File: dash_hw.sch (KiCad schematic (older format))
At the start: 25 parts, among them J1 Conn_01x06_Male, SW1 SW_Push, U1 STM32F103C8Tx, Y1 Crystal

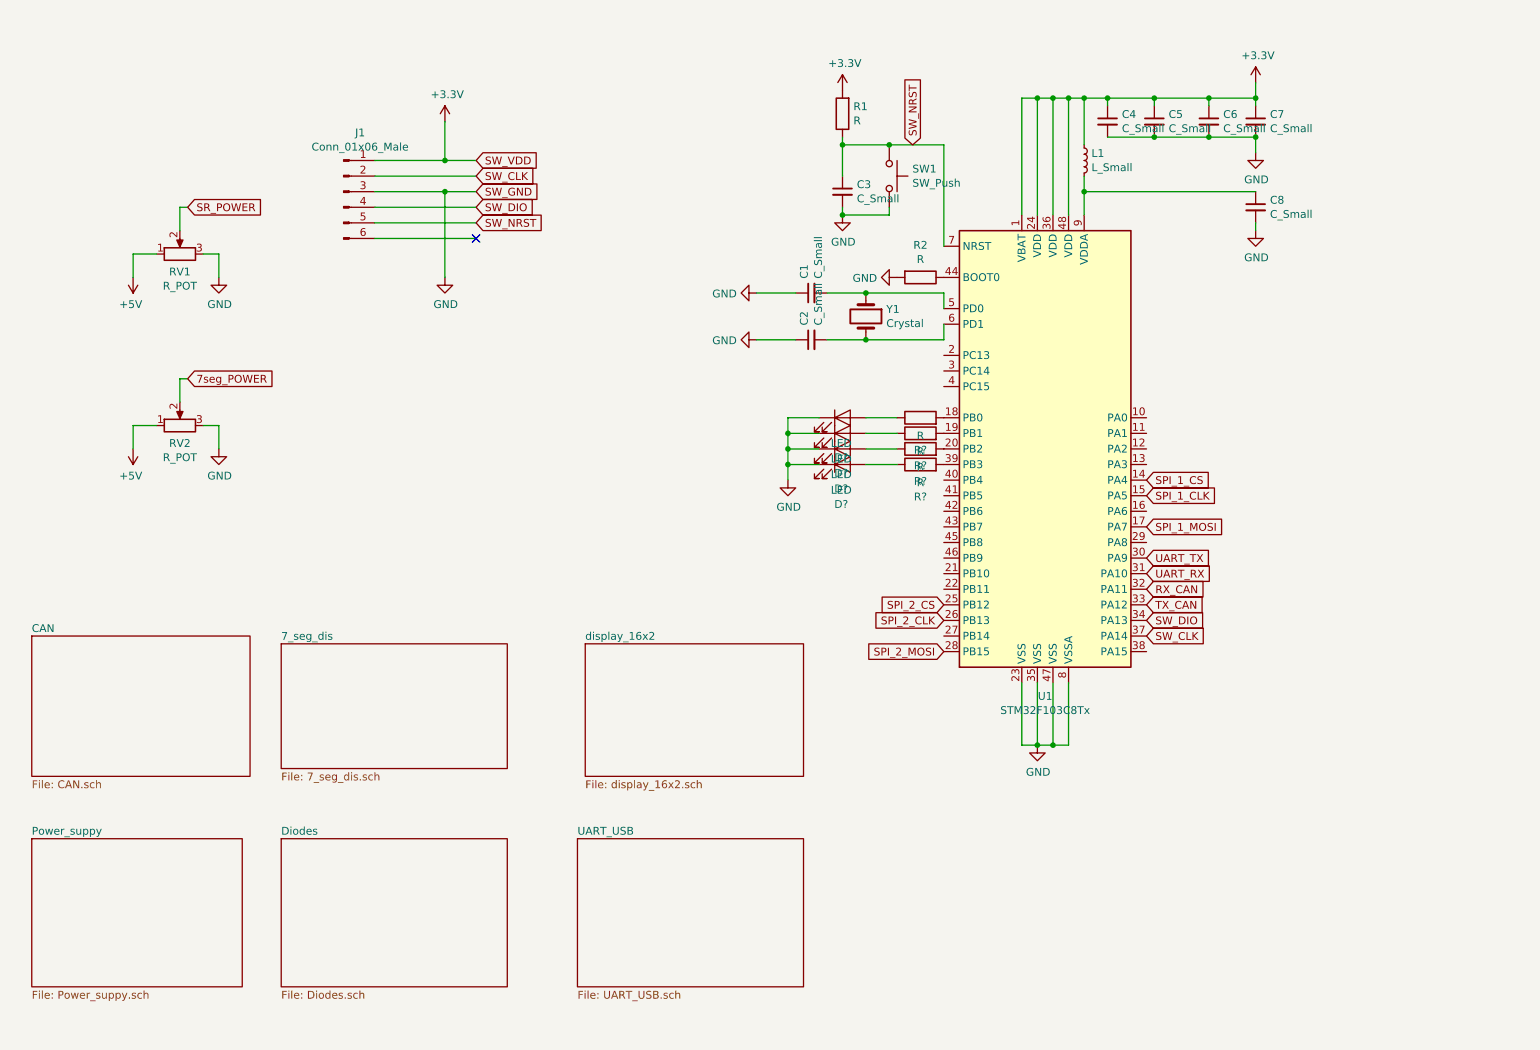
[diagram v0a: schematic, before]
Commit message: reorganized schematic; added reverse polarity protection; start adding footprints
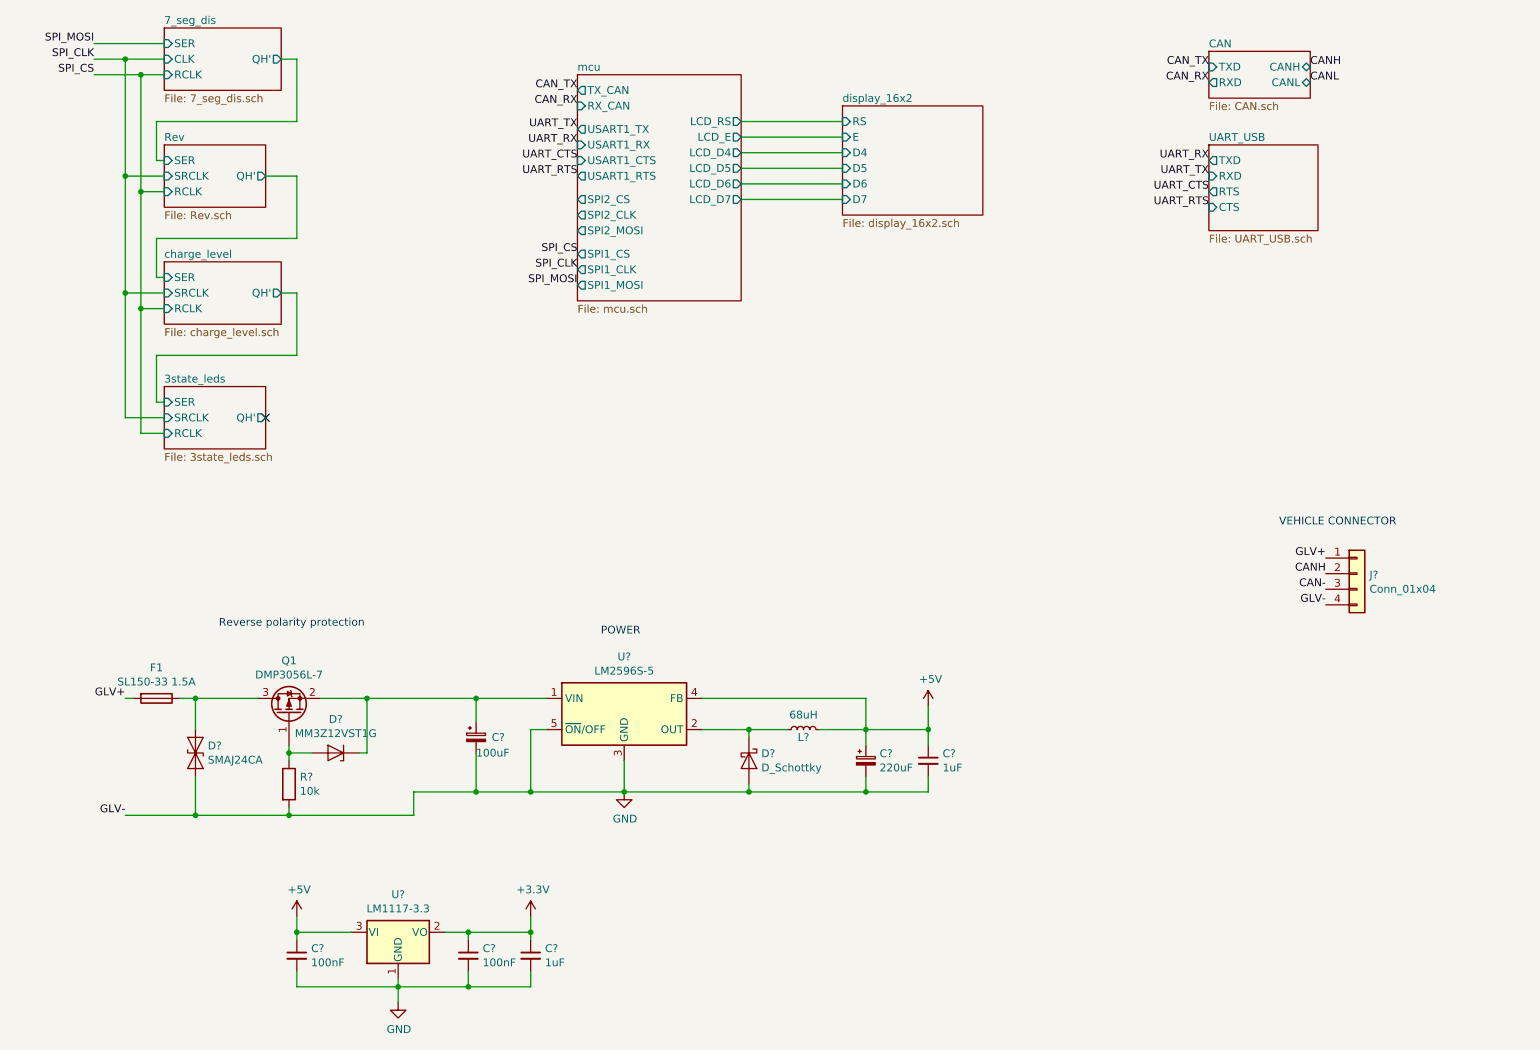
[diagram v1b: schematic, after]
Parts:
- removed C1, C2, C3, C4, C5, C6, C7, C8: C_Small, symbol Device:C_Small
- removed D? (x4): LED, symbol Device:LED
- removed J1: Conn_01x06_Male, symbol Connector:Conn_01x06_Male
- removed L1: L_Small, symbol Device:L_Small
- removed R1, R2, R? (x4): R, symbol Device:R
- removed RV1, RV2: R_POT, symbol Device:R_POT
- removed SW1: SW_Push, symbol Switch:SW_Push
- removed U1: STM32F103C8Tx, Package_QFP:LQFP-48_7x7mm_P0.5mm, symbol MCU_ST_STM32F1:STM32F103C8Tx
- removed Y1: Crystal, symbol Device:Crystal
- added C? (x2): 1uF, symbol Device:C_Small
- added C?: 100uF, symbol Device:CP_Small
- added C?: 220uF, symbol Device:CP_Small
- added C? (x2): 100nF, symbol Device:C_Small
- added D?: D_Schottky, symbol Device:D_Schottky
- added D?: SMAJ24CA, Diode_SMD:D_SMA, symbol Device:D_TVS
- added D?: MM3Z12VST1G, Diode_SMD:D_SOD-323, symbol Device:D_Zener
- added F1: SL150-33 1.5A, Fuse:Fuse_2920_7451Metric, symbol Device:Fuse
- added J?: Conn_01x04, symbol Connector_Generic:Conn_01x04
- added L?: 68uH, Inductor_SMD:L_10.4x10.4_H4.8, symbol Device:L_Small
- added Q1: DMP3056L-7, Package_TO_SOT_SMD:SOT-23, symbol Device:Q_PMOS_GSD
- added R?: 10k, symbol Device:R
- added U?: LM2596S-5, Package_TO_SOT_SMD:TO-263-5_TabPin3, symbol Regulator_Switching:LM2596S-5
- added U?: LM1117-3.3, symbol Regulator_Linear:LM1117-3.3
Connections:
- net +3V3: now also C?.1, C?.1, U?.2 (VO)
- net +5V: now also C?.1, C?.1, C?.1, L?.2, U?.3 (VI), U?.4 (FB)
- net GND: now also C?.2, C?.2, C?.2, C?.2, C?.2, C?.2, D?.2 (A), D?.2 (A2), J?.4 (Pin_4), R?.2, U?.1 (GND), U?.3 (GND), U?.5 (~ON~/OFF)
- new net: C?.1, D?.1 (K), Q1.2 (S), U?.1 (VIN)
- new net: D?.1 (K), L?.1, U?.2 (OUT)
- new net: D?.1 (A1), F1.1, Q1.3 (D)
- new net: D?.2 (A), Q1.1 (G), R?.1
- new net CAN-: J?.3 (Pin_3)
- new net CANH: J?.2 (Pin_2)
- new net GLV+: F1.2, J?.1 (Pin_1)
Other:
- note added: "POWER"
- note added: "Reverse polarity protection"
- note added: "VEHICLE CONNECTOR"

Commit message: footprints; library for 7seg; start pcb layout
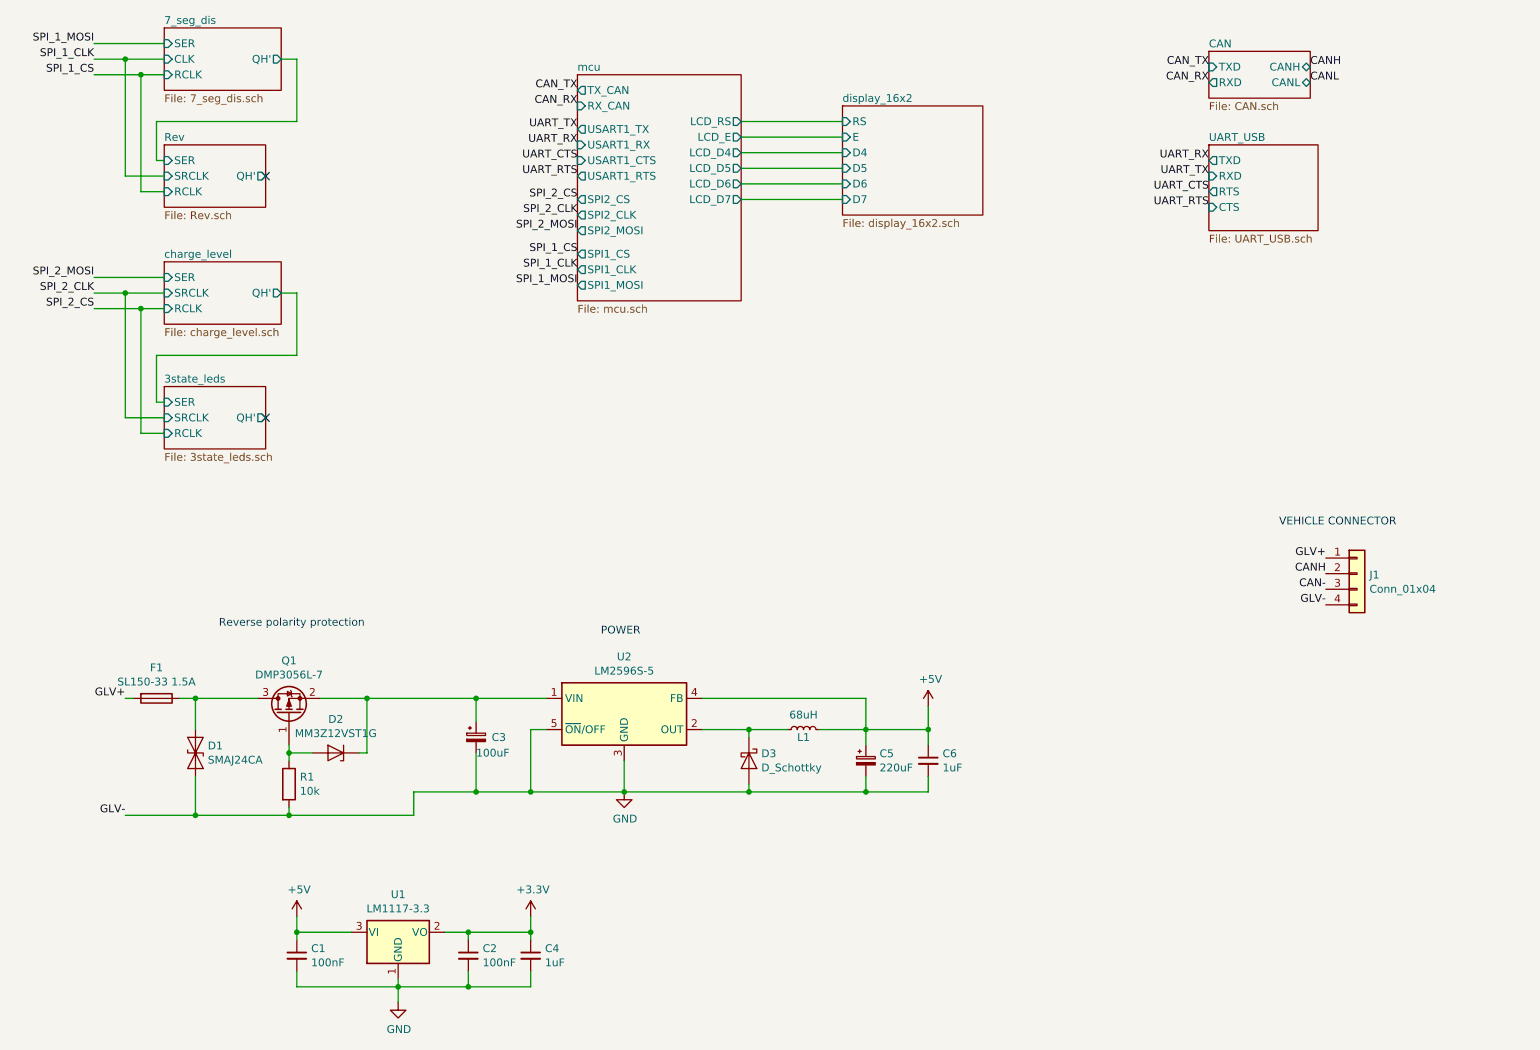
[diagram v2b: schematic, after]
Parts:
- C1, C2, C4, C6: renamed from C?; footprint (none) -> Capacitor_SMD:C_0603_1608Metric
- C3, C5: renamed from C?; footprint (none) -> Capacitor_SMD:CP_Elec_8x10
- D3: renamed from D?; footprint (none) -> Diode_SMD:D_SMB
- J1: renamed from J?; footprint (none) -> Connector_PinHeader_2.54mm:PinHeader_1x04_P2.54mm_Vertical
- R1: renamed from R?; footprint (none) -> Resistor_SMD:R_0603_1608Metric
- U1: renamed from U?; footprint (none) -> Package_TO_SOT_SMD:SOT-223-3_TabPin2
- gave numbers to parts that had none: 4
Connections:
- no-connect marks 1 -> 2
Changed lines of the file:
@@
 Wire Wire Line
 	1600 1450 1600 1700
-Text Label 1200 950  2    50   ~ 0
-SPI_MOSI
-Text Label 1200 1050 2    50   ~ 0
-SPI_CLK
-Text Label 1200 1150 2    50   ~ 0
-SPI_CS
 Text Label 4300 2500 2    50   ~ 0
-SPI_MOSI
+SPI_1_MOSI
 Text Label 4300 2400 2    50   ~ 0
-SPI_CLK
+SPI_1_CLK
 Text Label 4300 2300 2    50   ~ 0
-SPI_CS
+SPI_1_CS
 Wire Wire Line
 	1200 950  1650 950
@@
 	1500 1150 1650 1150
 Wire Wire Line
-	1500 1900 1500 2650
-Wire Wire Line
-	1500 2650 1650 2650
-Connection ~ 1500 1900
-Wire Wire Line
-	1650 2450 1600 2450
-Wire Wire Line
-	1600 2450 1600 2200
-Wire Wire Line
-	1600 2200 2500 2200
-Wire Wire Line
-	2500 2200 2500 1800
-Wire Wire Line
-	2500 1800 2300 1800
-Wire Wire Line
 	1600 1700 1650 1700
 Wire Wire Line
-	1500 2650 1500 3450
-Wire Wire Line
 	1500 3450 1650 3450
-Connection ~ 1500 2650
 Wire Wire Line
 	2400 2550 2500 2550
@@
 Wire Wire Line
 	1650 3350 1400 3350
-Wire Wire Line
-	1400 3350 1400 2550
 Connection ~ 1400 1050
 Wire Wire Line
@@
 Wire Wire Line
 	1650 1800 1400 1800
-Connection ~ 1400 1800
 Wire Wire Line
 	1400 1800 1400 1050
-Wire Wire Line
-	1650 2550 1400 2550
-Connection ~ 1400 2550
-Wire Wire Line
-	1400 2550 1400 1800
 $Comp
 L Regulator_Switching:LM2596S-5 U?
@@
 P 4600 5250
 AR Path="/61C146B0/5FD2508C" Ref="U?"  Part="1"
-AR Path="/5FD2508C" Ref="U?"  Part="1"
-F 0 "U?" H 4600 5617 50  0000 C CNN
+AR Path="/5FD2508C" Ref="U2"  Part="1"
+F 0 "U2" H 4600 5617 50  0000 C CNN
 F 1 "LM2596S-5" H 4600 5526 50  0000 C CNN
 F 2 "Package_TO_SOT_SMD:TO-263-5_TabPin3" H 4650 5000 50  0001 L CIN
@@
 P 6550 5550
 AR Path="/61C146B0/5FD250AD" Ref="C?"  Part="1"
-AR Path="/5FD250AD" Ref="C?"  Part="1"
-F 0 "C?" H 6642 5596 50  0000 L CNN
+AR Path="/5FD250AD" Ref="C6"  Part="1"
+F 0 "C6" H 6642 5596 50  0000 L CNN
 F 1 "1uF" H 6642 5505 50  0000 L CNN
-F 2 "" H 6550 5550 50  0001 C CNN
+F 2 "Capacitor_SMD:C_0603_1608Metric" H 6550 5550 50  0001 C CNN
 F 3 "~" H 6550 5550 50  0001 C CNN
 	1    6550 5550
@@
 P 3650 5400
 AR Path="/61C146B0/5FD250B3" Ref="C?"  Part="1"
-AR Path="/5FD250B3" Ref="C?"  Part="1"
-F 0 "C?" H 3750 5400 50  0000 L CNN
+AR Path="/5FD250B3" Ref="C3"  Part="1"
+F 0 "C3" H 3750 5400 50  0000 L CNN
 F 1 "100uF" H 3650 5300 50  0000 L CNN
-F 2 "" H 3650 5400 50  0001 C CNN
+F 2 "Capacitor_SMD:CP_Elec_8x10" H 3650 5400 50  0001 C CNN
 F 3 "~" H 3650 5400 50  0001 C CNN
 	1    3650 5400
@@
 P 4600 5750
 AR Path="/61C146B0/5FD250B9" Ref="#PWR?"  Part="1"
-AR Path="/5FD250B9" Ref="#PWR?"  Part="1"
-F 0 "#PWR?" H 4600 5500 50  0001 C CNN
+AR Path="/5FD250B9" Ref="#PWR04"  Part="1"
+F 0 "#PWR04" H 4600 5500 50  0001 C CNN
 F 1 "GND" H 4605 5577 50  0000 C CNN
 F 2 "" H 4600 5750 50  0001 C CNN
@@
 P 5400 5550
 AR Path="/61C146B0/5FD250C5" Ref="D?"  Part="1"
-AR Path="/5FD250C5" Ref="D?"  Part="1"
-F 0 "D?" V 5354 5629 50  0000 L CNN
+AR Path="/5FD250C5" Ref="D3"  Part="1"
+F 0 "D3" V 5354 5629 50  0000 L CNN
 F 1 "D_Schottky" V 5445 5629 50  0000 L CNN
-F 2 "" H 5400 5550 50  0001 C CNN
+F 2 "Diode_SMD:D_SMB" H 5400 5550 50  0001 C CNN
 F 3 "~" H 5400 5550 50  0001 C CNN
 	1    5400 5550
@@
 P 5750 5350
 AR Path="/61C146B0/5FD250CB" Ref="L?"  Part="1"
-AR Path="/5FD250CB" Ref="L?"  Part="1"
-F 0 "L?" V 5700 5350 50  0000 C CNN
+AR Path="/5FD250CB" Ref="L1"  Part="1"
+F 0 "L1" V 5700 5350 50  0000 C CNN
 F 1 "68uH" V 5844 5350 50  0000 C CNN
 F 2 "Inductor_SMD:L_10.4x10.4_H4.8" H 5750 5350 50  0001 C CNN
@@
 P 6150 5550
 AR Path="/61C146B0/5FD250D1" Ref="C?"  Part="1"
-AR Path="/5FD250D1" Ref="C?"  Part="1"
-F 0 "C?" H 6238 5596 50  0000 L CNN
+AR Path="/5FD250D1" Ref="C5"  Part="1"
+F 0 "C5" H 6238 5596 50  0000 L CNN
 F 1 "220uF" H 6238 5505 50  0000 L CNN
-F 2 "" H 6150 5550 50  0001 C CNN
+F 2 "Capacitor_SMD:CP_Elec_8x10" H 6150 5550 50  0001 C CNN
 F 3 "~" H 6150 5550 50  0001 C CNN
 	1    6150 5550
@@
 P 6550 5200
 AR Path="/61C146B0/5FD250E2" Ref="#PWR?"  Part="1"
-AR Path="/5FD250E2" Ref="#PWR?"  Part="1"
-F 0 "#PWR?" H 6550 5050 50  0001 C CNN
+AR Path="/5FD250E2" Ref="#PWR05"  Part="1"
+F 0 "#PWR05" H 6550 5050 50  0001 C CNN
 F 1 "+5V" H 6565 5373 50  0000 C CNN
 F 2 "" H 6550 5200 50  0001 C CNN
@@
 P 3150 6650
 AR Path="/61C146B0/5FD250E8" Ref="U?"  Part="1"
-AR Path="/5FD250E8" Ref="U?"  Part="1"
-F 0 "U?" H 3150 6892 50  0000 C CNN
+AR Path="/5FD250E8" Ref="U1"  Part="1"
+F 0 "U1" H 3150 6892 50  0000 C CNN
 F 1 "LM1117-3.3" H 3150 6801 50  0000 C CNN
-F 2 "" H 3150 6650 50  0001 C CNN
+F 2 "Package_TO_SOT_SMD:SOT-223-3_TabPin2" H 3150 6650 50  0001 C CNN
 F 3 "http://www.ti.com/lit/ds/symlink/lm1117.pdf" H 3150 6650 50  0001 C CNN
 	1    3150 6650
@@
 P 2500 6550
 AR Path="/61C146B0/5FD250EE" Ref="#PWR?"  Part="1"
-AR Path="/5FD250EE" Ref="#PWR?"  Part="1"
-F 0 "#PWR?" H 2500 6400 50  0001 C CNN
+AR Path="/5FD250EE" Ref="#PWR01"  Part="1"
+F 0 "#PWR01" H 2500 6400 50  0001 C CNN
 F 1 "+5V" H 2515 6723 50  0000 C CNN
 F 2 "" H 2500 6550 50  0001 C CNN
@@
 P 2500 6800
 AR Path="/61C146B0/5FD250F4" Ref="C?"  Part="1"
-AR Path="/5FD250F4" Ref="C?"  Part="1"
-F 0 "C?" H 2592 6846 50  0000 L CNN
+AR Path="/5FD250F4" Ref="C1"  Part="1"
+F 0 "C1" H 2592 6846 50  0000 L CNN
 F 1 "100nF" H 2592 6755 50  0000 L CNN
-F 2 "" H 2500 6800 50  0001 C CNN
+F 2 "Capacitor_SMD:C_0603_1608Metric" H 2500 6800 50  0001 C CNN
 F 3 "~" H 2500 6800 50  0001 C CNN
 	1    2500 6800
@@
 P 3600 6800
 AR Path="/61C146B0/5FD250FA" Ref="C?"  Part="1"
-AR Path="/5FD250FA" Ref="C?"  Part="1"
-F 0 "C?" H 3692 6846 50  0000 L CNN
+AR Path="/5FD250FA" Ref="C2"  Part="1"
+F 0 "C2" H 3692 6846 50  0000 L CNN
 F 1 "100nF" H 3692 6755 50  0000 L CNN
-F 2 "" H 3600 6800 50  0001 C CNN
+F 2 "Capacitor_SMD:C_0603_1608Metric" H 3600 6800 50  0001 C CNN
 F 3 "~" H 3600 6800 50  0001 C CNN
 	1    3600 6800
@@
 P 3150 7100
 AR Path="/61C146B0/5FD25100" Ref="#PWR?"  Part="1"
-AR Path="/5FD25100" Ref="#PWR?"  Part="1"
-F 0 "#PWR?" H 3150 6850 50  0001 C CNN
+AR Path="/5FD25100" Ref="#PWR02"  Part="1"
+F 0 "#PWR02" H 3150 6850 50  0001 C CNN
 F 1 "GND" H 3155 6927 50  0000 C CNN
 F 2 "" H 3150 7100 50  0001 C CNN
@@
 P 4000 6550
 AR Path="/61C146B0/5FD25107" Ref="#PWR?"  Part="1"
-AR Path="/5FD25107" Ref="#PWR?"  Part="1"
-F 0 "#PWR?" H 4000 6400 50  0001 C CNN
+AR Path="/5FD25107" Ref="#PWR03"  Part="1"
+F 0 "#PWR03" H 4000 6400 50  0001 C CNN
 F 1 "+3.3V" H 4015 6723 50  0000 C CNN
 F 2 "" H 4000 6550 50  0001 C CNN
@@
 POWER
 $Comp
-L Device:D_TVS D?
+L Device:D_TVS D1
 U 1 1 5FD4D349
 P 1850 5500
-F 0 "D?" V 1804 5579 50  0000 L CNN
+F 0 "D1" V 1804 5579 50  0000 L CNN
 F 1 "SMAJ24CA" V 1895 5579 50  0000 L CNN
 F 2 "Diode_SMD:D_SMA" H 1850 5500 50  0001 C CNN
@@
 P 4000 6800
 AR Path="/61C146B0/5FD6239C" Ref="C?"  Part="1"
-AR Path="/5FD6239C" Ref="C?"  Part="1"
-F 0 "C?" H 4092 6846 50  0000 L CNN
+AR Path="/5FD6239C" Ref="C4"  Part="1"
+F 0 "C4" H 4092 6846 50  0000 L CNN
 F 1 "1uF" H 4092 6755 50  0000 L CNN
-F 2 "" H 4000 6800 50  0001 C CNN
+F 2 "Capacitor_SMD:C_0603_1608Metric" H 4000 6800 50  0001 C CNN
 F 3 "~" H 4000 6800 50  0001 C CNN
 	1    4000 6800
@@
 	1850 5150 1850 5350
 $Comp
-L Device:R R?
+L Device:R R1
 U 1 1 5FD84941
 P 2450 5700
-F 0 "R?" H 2520 5746 50  0000 L CNN
+F 0 "R1" H 2520 5746 50  0000 L CNN
 F 1 "10k" H 2520 5655 50  0000 L CNN
-F 2 "" V 2380 5700 50  0001 C CNN
+F 2 "Resistor_SMD:R_0603_1608Metric" V 2380 5700 50  0001 C CNN
 F 3 "~" H 2450 5700 50  0001 C CNN
 	1    2450 5700
@@
 	2450 5550 2450 5500
 $Comp
-L Device:D_Zener D?
+L Device:D_Zener D2
 U 1 1 5FD8CF67
 P 2750 5500
-F 0 "D?" H 2750 5284 50  0000 C CNN
+F 0 "D2" H 2750 5284 50  0000 C CNN
 F 1 "MM3Z12VST1G" H 2750 5375 50  0000 C CNN
 F 2 "Diode_SMD:D_SOD-323" H 2750 5500 50  0001 C CNN
@@
 NoConn ~ 2300 3350
 $Comp
-L Connector_Generic:Conn_01x04 J?
+L Connector_Generic:Conn_01x04 J1
 U 1 1 5FDE07F9
 P 9300 4350
-F 0 "J?" H 9380 4342 50  0000 L CNN
+F 0 "J1" H 9380 4342 50  0000 L CNN
 F 1 "Conn_01x04" H 9380 4251 50  0000 L CNN
-F 2 "" H 9300 4350 50  0001 C CNN
+F 2 "Connector_PinHeader_2.54mm:PinHeader_1x04_P2.54mm_Vertical" H 9300 4350 50  0001 C CNN
 F 3 "~" H 9300 4350 50  0001 C CNN
 	1    9300 4350
@@
 	0    -1   -1   0
 $EndComp
+Text Label 4300 2150 2    50   ~ 0
+SPI_2_MOSI
+Text Label 4300 2050 2    50   ~ 0
+SPI_2_CLK
+Text Label 4300 1950 2    50   ~ 0
+SPI_2_CS
+Text Label 1200 950  2    50   ~ 0
+SPI_1_MOSI
+Text Label 1200 1050 2    50   ~ 0
+SPI_1_CLK
+Text Label 1200 1150 2    50   ~ 0
+SPI_1_CS
+NoConn ~ 2300 1800
+Text Label 1200 2450 2    50   ~ 0
+SPI_2_MOSI
+Text Label 1200 2550 2    50   ~ 0
+SPI_2_CLK
+Text Label 1200 2650 2    50   ~ 0
+SPI_2_CS
+Wire Wire Line
+	1200 2450 1650 2450
+Wire Wire Line
+	1200 2550 1400 2550
+Wire Wire Line
+	1200 2650 1500 2650
+Wire Wire Line
+	1400 3350 1400 2550
+Connection ~ 1400 2550
+Wire Wire Line
+	1400 2550 1650 2550
+Wire Wire Line
+	1500 2650 1500 3450
+Connection ~ 1500 2650
+Wire Wire Line
+	1500 2650 1650 2650
 $EndSCHEMATC
